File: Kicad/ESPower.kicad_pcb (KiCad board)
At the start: 2 copper layers, 84.6 x 14.5 mm, 35 parts, among them Q1 DMP2035U-7, Q2 FS8205A, SW2 A, SW3 B, U1 TP4056, U2 DW01A, U3 SPX3819M5-L-3-3, U4 TPS3839DBZ

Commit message: Final routing
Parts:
- moved C2 0.76 mm to (157.0, 100.7)
- moved C3 0.76 mm to (152.1, 104.8)
- moved C6 0.76 mm to (157.9, 97.2)
- moved C7 0.76 mm to (136.4, 103.3)
- moved ESP-01 0.76 mm to (155.9, 101.6)
- moved R9 0.76 mm to (142.1, 103.8)
- moved U3 0.76 mm to (156.8, 105.3)
- moved U4 0.76 mm to (153.9, 97.9)
- moved GPIO 0.25 mm to (131.1, 96.1)
- moved Power 0.25 mm to (131.0, 106.8)
- renumbered SW2 to A, SW3 to B, Batt+ to B+
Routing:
- net VDD: track 56.8 -> 55.7 mm
- net +3V3: track 37.8 -> 37.3 mm
- net Net-(J3-Pad2): track 31.0 -> 30.5 mm
- net Net-(J5-Pad2): track 18.1 -> 17.6 mm
- net Net-(J5-Pad3): track 23.8 -> 23.3 mm
- net Net-(J5-Pad1): track 25.5 -> 25.0 mm
- added copper zone on B.Cu, net GND
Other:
- board size 84.6 x 14.5 mm -> 82.4 x 15.2 mm
- board text added: "(cc) BY-NC-SA - 2022 www.agius-industries.eu"
- board text added: "+3.3V"
- board text added: "0"
- board text added: "0 0 250mA 0 1 330mA 1 0 500mA 1 1 1A"
- board text added: "0: VCC=Batt 1: VCC=Input|Batt"
- board text added: "2"
- board text added: "A B Current"
- board text added: "B-"
- board text added: "EN"
- board text added: "ESPower v1.0"
- board text added: "GND"
- board text added: "Rx.3"
- board text added: "Tx.1"
- board text added: "VCC"
- board text removed: "Batt-"
- board text removed: "TODO: Power path select On : Enable powerpath, Input 5V only off : Only battery, Input 5-8v (solar panel)"

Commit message: Pre-reorganization
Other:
- board text added: "."

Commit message: pre-change diode
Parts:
- added ?: MountingHole_2.7mm_M2.5, MountingHole:MountingHole_2.7mm_M2.5, F.Cu at (127.3, 101.6)
- moved R2 3.61 mm to (114.8, 99.9)
- moved C5 0.63 mm to (105.5, 99.2)
- moved R8 0.63 mm to (105.5, 101.1)
- moved Q2 0.51 mm to (110.9, 96.1)
- moved U2 0.51 mm to (111.1, 101.5)
- moved C1 0.25 mm to (119.3, 102.6)
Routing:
- net GND: track 48.7 -> 55.2 mm, vias 5 -> 4
- net Net-(Q2-Pad5): track 4.44 -> 5.79 mm
- net +BATT: track 16.1 -> 15.5 mm
- net Net-(C4-Pad1): track 8.06 -> 8.62 mm
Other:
- board text added: "3.3V"
- board text removed: "+3.3V"

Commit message: Switched diodes to SS34C
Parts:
- D1, D2: value MBRS320T3 -> SS34C; footprint Custom:DIOM7959X261N -> Diode_SMD:D_SMC
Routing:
- net Net-(R5-Pad1): track 13.2 -> 14.5 mm
- net GND: track 55.2 -> 55.9 mm

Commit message: Version 1.0
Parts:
- D1, D2: value SS34C -> SS34; footprint Diode_SMD:D_SMC -> Diode_SMD:D_SMA
- moved D1 6.33 mm to (89.4, 106.8)
- moved A 5.29 mm to (89.0, 103.3)
- moved B 5.29 mm to (89.0, 99.6)
- moved R5 4.70 mm to (86.9, 103.6), turned to 90 degrees
- moved GND 4.42 mm to (84.1, 97.3)
- moved R6 4.21 mm to (86.9, 99.9), turned to 90 degrees
- moved U1 3.94 mm to (96.8, 99.7)
- moved R7 3.86 mm to (86.9, 96.3), turned to 90 degrees
- moved R1 3.74 mm to (101.0, 101.6)
- moved R4 3.72 mm to (92.2, 101.1)
- moved D4 3.68 mm to (92.2, 97.3)
- moved R3 3.47 mm to (89.7, 101.1)
- moved D3 3.43 mm to (89.7, 97.3)
- moved Q1 3.35 mm to (103.9, 101.5)
- moved R8 3.15 mm to (108.0, 103.1), turned to 270 degrees
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- gave numbers to parts that had none: 1
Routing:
- net GND: track 55.9 -> 50.7 mm
- net Net-(D1-PadA): track 6.01 -> 9.95 mm
- net Net-(R5-Pad2): track 10.9 -> 7.04 mm
- net Net-(C4-Pad1): track 8.62 -> 5.87 mm
- net Net-(C1-Pad1): track 23.4 -> 20.6 mm
- net Net-(Q2-Pad5): track 5.79 -> 8.43 mm
- net Net-(C4-Pad2): track 22.3 -> 20.6 mm
- net +3V3: track 37.3 -> 36.0 mm
- net Net-(J3-Pad2): track 30.5 -> 29.3 mm
- net Net-(R6-Pad2): track 5.13 -> 6.24 mm
- net Net-(R2-Pad1): track 5.74 -> 4.67 mm
- net VDD: track 55.7 -> 54.7 mm
- net Net-(D3-Pad1): track 9.44 -> 10.3 mm
- net Net-(J5-Pad4): track 38.6 -> 37.8 mm
- net Net-(J5-Pad3): track 23.3 -> 22.5 mm
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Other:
- board size 82.4 x 15.2 mm -> 77 x 15 mm
- net class Default: trace_width 0.3 -> 0.4
- board text added: "On: VCC=Input|Batt Off: VCC=Batt"
- board text removed: "0: VCC=Batt 1: VCC=Input|Batt"

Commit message: Update to KiCad v6
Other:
- net class Default removed
- net class Power removed

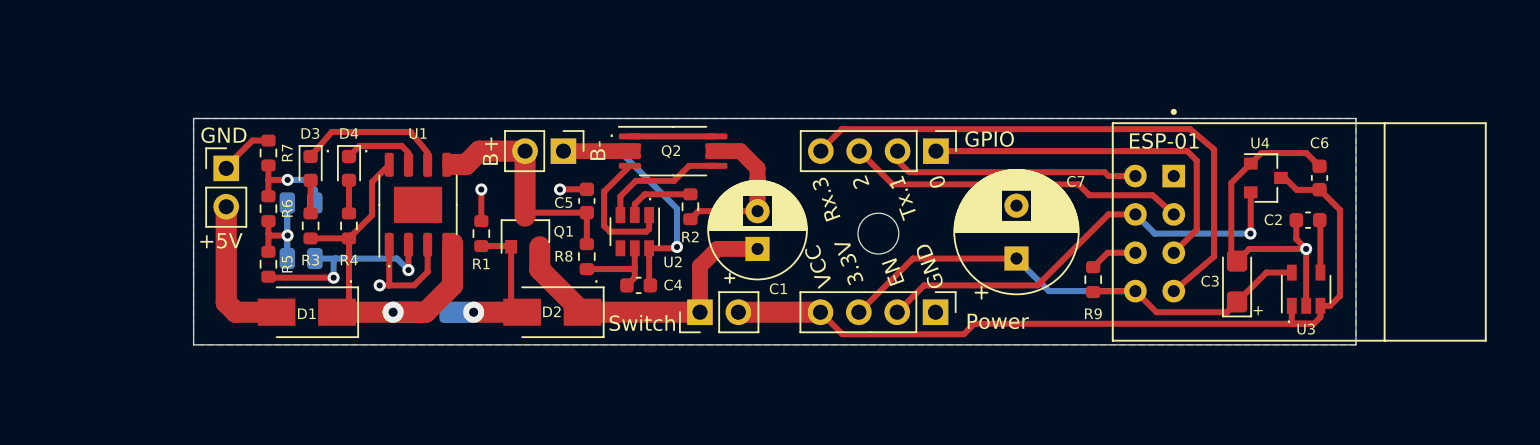
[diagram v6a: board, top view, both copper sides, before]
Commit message: Resized board
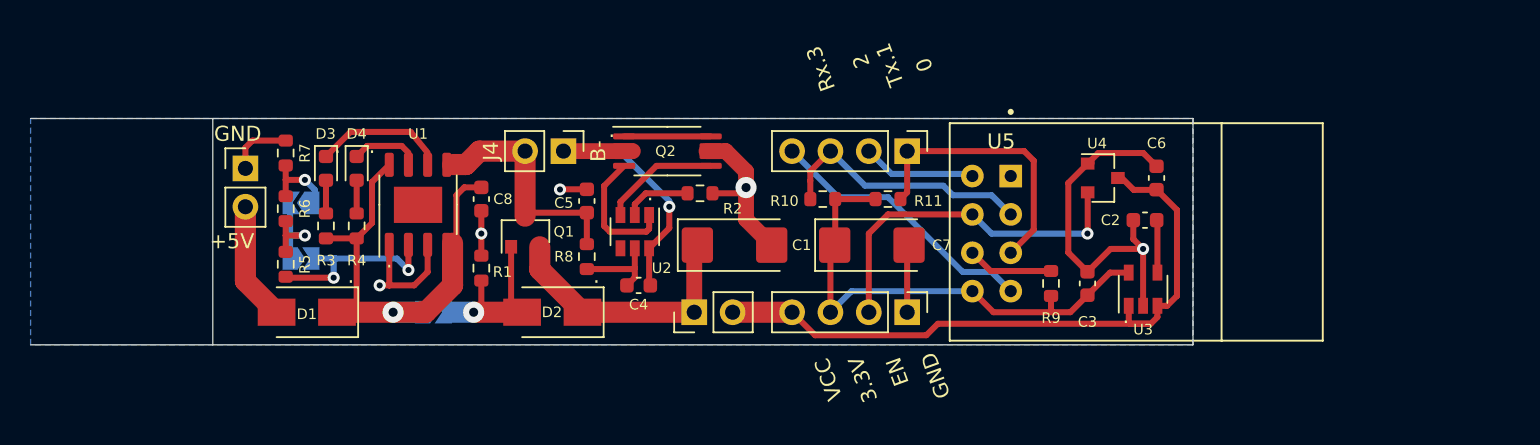
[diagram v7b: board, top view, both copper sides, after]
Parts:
- removed Hole1: MountingHole_2.7mm_M2.5, MountingHole:MountingHole_2.7mm_M2.5
- added C8: 10uF, Capacitor_SMD:C_0603_1608Metric, F.Cu at (101.0, 99.3)
- added R10: 10k, Resistor_SMD:R_0603_1608Metric, F.Cu at (123.6, 99.3)
- added R11: 10k, Resistor_SMD:R_0603_1608Metric, F.Cu at (127.9, 99.3)
- C1: value 220µF -> 220uF; footprint Capacitor_THT:CP_Radial_D6.3mm_P2.50mm -> Capacitor_Tantalum_SMD:CP_EIA-6032-28_Kemet-C
- C3: value 10µF -> 10uF; footprint Capacitor_Tantalum_SMD:CP_EIA-3216-10_Kemet-I -> Capacitor_SMD:C_0603_1608Metric
- C5: value 10µF -> 10uF
- C7: value 470µF -> 220uF; footprint Capacitor_THT:CP_Radial_D8.0mm_P3.50mm -> Capacitor_Tantalum_SMD:CP_EIA-6032-28_Kemet-C
- R1, R9: value 100kΩ -> 100k
- R2, R3, R4: value 1kΩ -> 1k
- R5: value 2.4kΩ -> 2.4k
- R6, R7: value 1.2kΩ -> 1.2k
- R8: value 100Ω -> 100
- SW1: renamed from Power Path; footprint Resistor_SMD:R_0805_2012Metric -> Jumper:SolderJumper-2_P1.3mm_Open_TrianglePad1.0x1.5mm
- SW2: renamed from A; footprint Resistor_SMD:R_0805_2012Metric -> Jumper:SolderJumper-2_P1.3mm_Open_TrianglePad1.0x1.5mm
- SW3: renamed from B; footprint Resistor_SMD:R_0805_2012Metric -> Jumper:SolderJumper-2_P1.3mm_Open_TrianglePad1.0x1.5mm
- U2: value DW01A -> (none)
- U4: value TPS3839DBZ -> TPS3839G33DBZ
- moved U5 10.8 mm to (144.3, 101.6)
- moved C2 10.8 mm to (144.9, 100.7)
- moved C6 10.8 mm to (145.7, 97.9)
- moved U3 10.8 mm to (144.8, 105.3)
- moved U4 10.8 mm to (142.1, 97.9)
- moved C3 9.91 mm to (141.1, 104.9)
- moved C7 9.62 mm to (126.8, 102.4), turned to 0 degrees
- moved R9 2.81 mm to (138.7, 104.9)
- moved R1 2.29 mm to (101.0, 103.9)
- moved J5 1.91 mm to (129.2, 96.1)
- moved J3 1.88 mm to (129.2, 106.8)
- moved C1 1.55 mm to (117.7, 102.4), turned to 0 degrees
- moved J1 1.27 mm to (85.3, 97.3)
- moved R5 1.14 mm to (88.0, 103.6)
- moved R6 1.14 mm to (88.0, 99.9)
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- renumbered GND to J1, Switch to J2, Power to J3, B+ to J4, GPIO to J5, ESP-01 to U5
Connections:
- U1 pad 9: Net-(U1-Pad9) -> unconnected-(U1-Pad9)
- U2 pad 4: Net-(U2-Pad4) -> unconnected-(U2-Pad4)
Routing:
- net Net-(J5-Pad4): track 37.8 -> 18.3 mm
- net VDD: track 54.7 -> 44.3 mm
- net Net-(J5-Pad2): track 16.8 -> 7.53 mm
- net GND: track 50.7 -> 56.6 mm, vias 4 -> 5
- net Net-(J3-Pad2): track 29.3 -> 23.5 mm
- net Net-(J5-Pad1): track 24.3 -> 18.7 mm
- net Net-(J5-Pad3): track 22.5 -> 17.5 mm
- net +5V: track 26.7 -> 31.2 mm
- net Net-(C1-Pad1): track 20.6 -> 17.4 mm
- net +3V3: track 36.0 -> 33.4 mm
- net Net-(R9-Pad2): track 3.19 -> 5.71 mm
- net Net-(D1-Pad2): track 9.95 -> 7.84 mm
- net Net-(C4-Pad2): track 20.6 -> 19.1 mm
- net Net-(R6-Pad2): track 6.24 -> 5.10 mm
- net Net-(R5-Pad1): track 14.5 -> 13.4 mm
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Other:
- outline, holes or cut-outs redrawn
- board text removed: "+"

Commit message: Finalized silkscreen
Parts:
- moved J1 2.41 mm to (85.3, 99.7)
- moved R9 1.14 mm to (139.2, 105.9)
- moved C3 1.05 mm to (141.4, 105.9)
- moved J2 0.51 mm to (115.1, 106.3)
- moved J3 0.51 mm to (129.2, 106.3)
- moved C1 0.38 mm to (117.7, 102.0)
- moved C7 0.38 mm to (126.8, 102.0)
- moved R5 0.25 mm to (88.0, 103.4)
- moved C5 0.25 mm to (108.0, 99.7)
- moved R10 0.25 mm to (123.6, 99.1)
- moved R11 0.25 mm to (127.9, 99.1)
- moved R6 0.13 mm to (88.0, 99.8)
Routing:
- net Net-(J5-Pad4): track 18.3 -> 28.3 mm
- net Net-(R9-Pad2): track 5.71 -> 9.50 mm
- net Net-(D1-Pad2): track 7.84 -> 5.43 mm
- net GND: track 56.6 -> 58.1 mm
- net Net-(R5-Pad1): track 13.4 -> 12.3 mm
- net Net-(J3-Pad2): track 23.5 -> 22.7 mm
- net +3V3: track 33.4 -> 34.2 mm
- net VDD: track 44.3 -> 43.6 mm
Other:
- board size 77 x 15 mm -> 64.9 x 15 mm
- board text added: "+"
- board text added: "-"
- board text added: "3"
- board text added: "3.3"
- board text added: "A"
- board text added: "B"
- board text added: "B+"
- board text added: "Batt"
- board text added: "ESPower v2.0"
- board text added: "Enable"
- board text added: "GPIO"
- board text added: "Power Path"
- board text added: "Switch"
- board text added: "e"
- board text removed: "EN"
- board text removed: "ESPower v1.0"
